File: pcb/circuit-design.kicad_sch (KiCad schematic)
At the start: 8 parts, among them J1 USB_C_Receptacle_USB2.0_16P, U1 USBLC6-2SC6

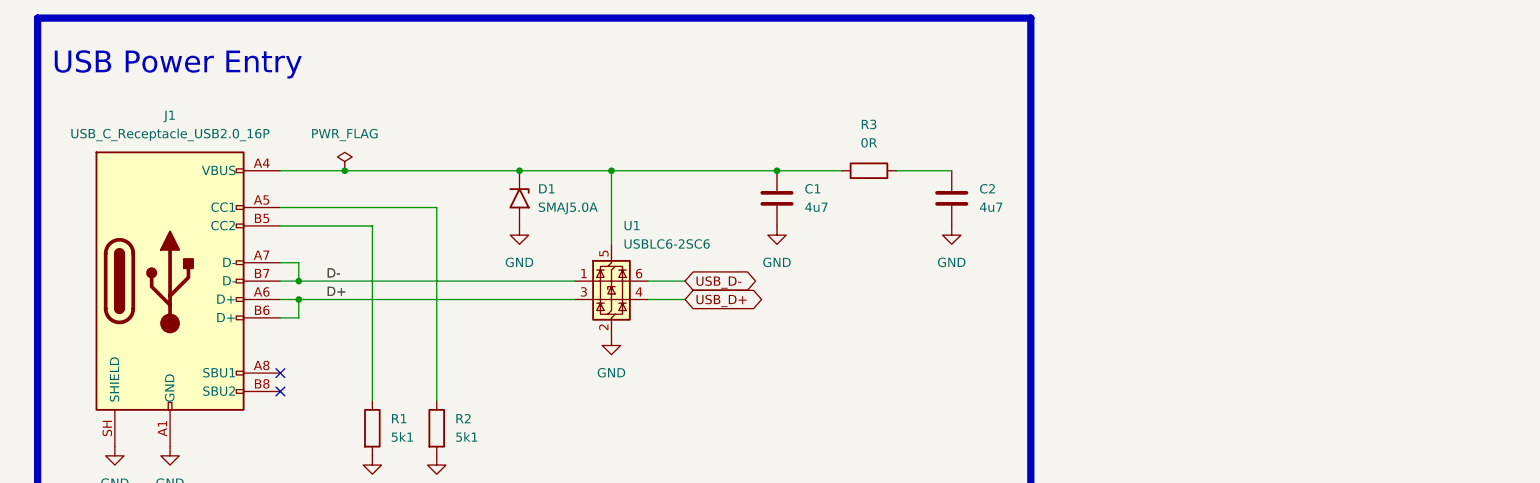
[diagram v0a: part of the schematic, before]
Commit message: feat(sch/pwr): add 3.3V LDO regulation circuit
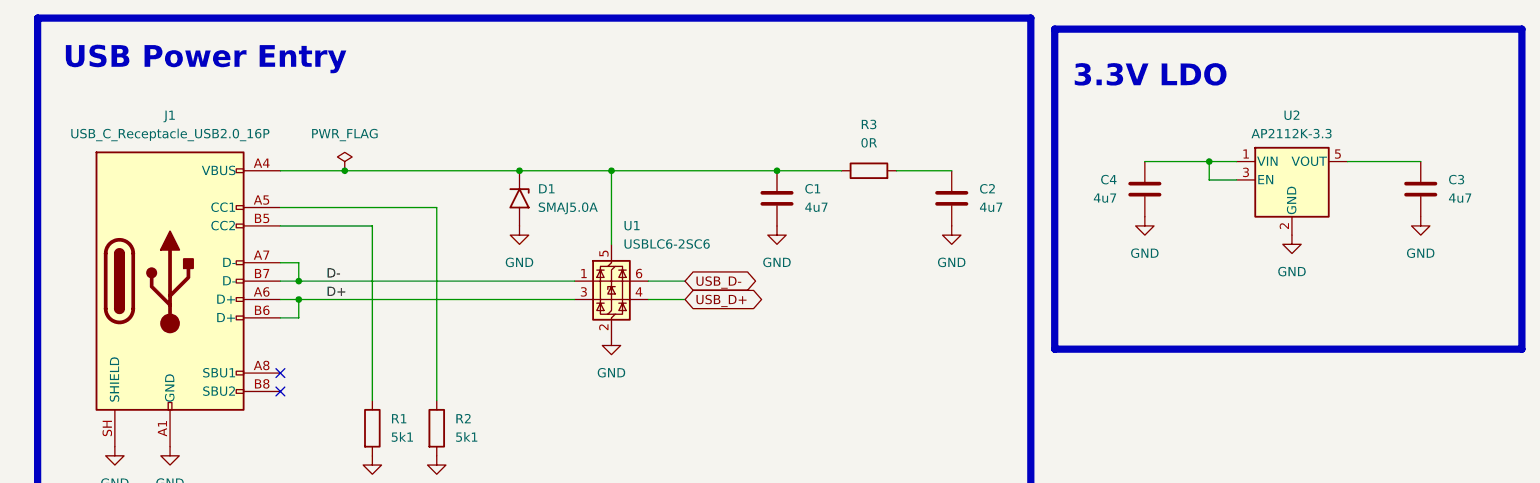
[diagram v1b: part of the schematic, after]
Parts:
- added C3, C4: 4u7, Package_TO_SOT_SMD:SOT-23-5, symbol Device:C
- added U2: AP2112K-3.3, Package_TO_SOT_SMD:SOT-23-5, symbol Regulator_Linear:AP2112K-3.3
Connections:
- net GND: now also C3.2, C4.2, U2.2 (GND)
- new net: C4.1, U2.1 (VIN), U2.3 (EN)
- new net: C3.1, U2.5 (VOUT)
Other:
- note added: "3.3V LDO"

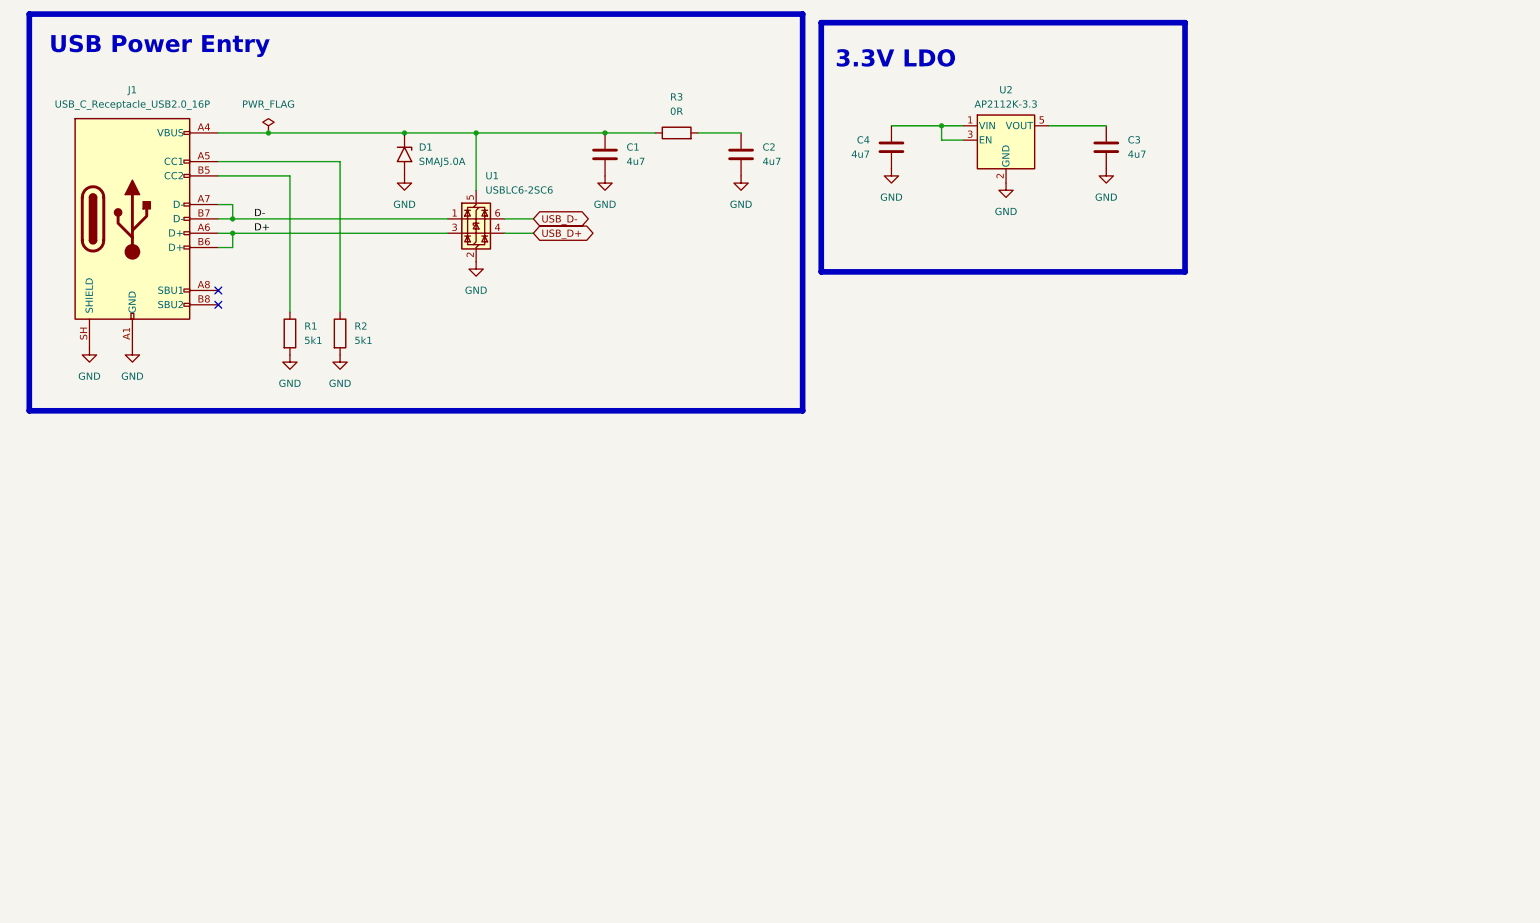
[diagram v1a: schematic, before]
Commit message: feat(sch/mcu): add mcu and auxiliary circuits
There were added the fundamental MCU circuits:
- Power conditioning
- Boot
- Reset/Enable (is the same for ESP32 MCUs)
- Clock
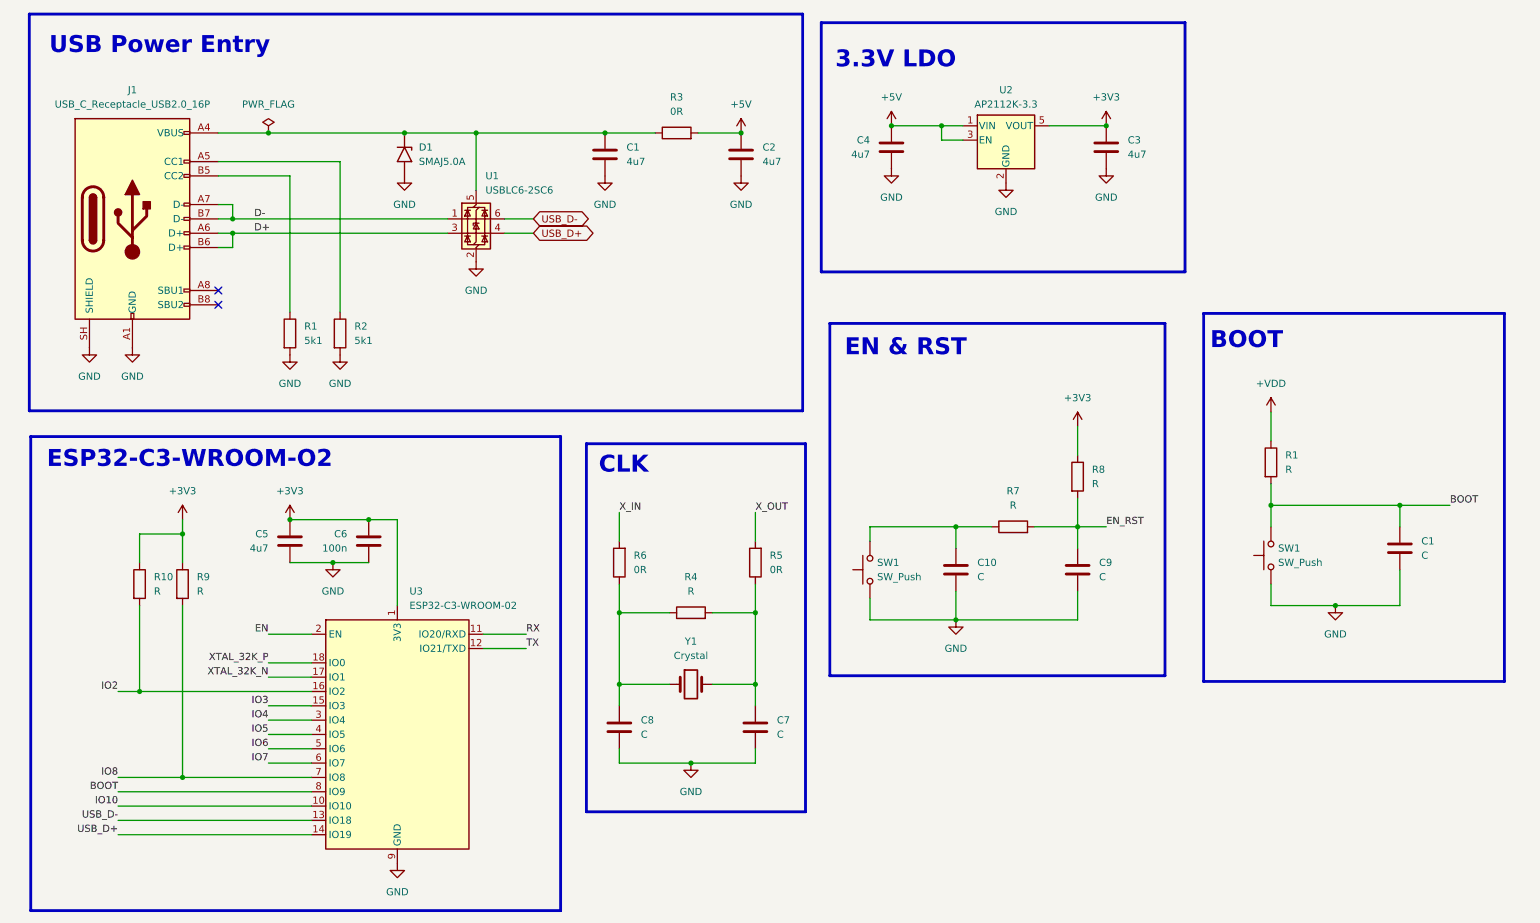
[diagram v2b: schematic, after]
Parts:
- added C1, C10, C7, C8, C9: C, symbol Device:C
- added C5: 4u7, Diode_SMD:D_SMA, symbol Device:C
- added C6: 100n, Diode_SMD:D_SMA, symbol Device:C
- added R1, R10, R4, R7, R8, R9: R, symbol Device:R
- added R5, R6: 0R, symbol Device:R
- added SW1 (x2): SW_Push, Button_Switch_SMD:Nidec_Copal_CAS-120A, symbol Switch:SW_Push
- added U3: ESP32-C3-WROOM-02, RF_Module:ESP32-C3-WROOM-02, symbol RF_Module:ESP32-C3-WROOM-02
- added Y1: Crystal, AMDY:XTAL_EPSON_TSX-3225, symbol Device:Crystal
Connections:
- net GND: now also C1.2, C10.2, C5.2, C6.2, C7.2, C8.2, C9.2, SW1.1, SW1.1, U3.19 (GND), U3.9 (GND)
- net USB_D+: now also U3.14 (IO19)
- net USB_D-: now also U3.13 (IO18)
- net +5V: now reaches C2.1, R3.2
- net +5V: now also C4.1, U2.1 (VIN), U2.3 (EN)
- net +3V3: now reaches C3.1, U2.5 (VOUT)
- net +3V3: now also C5.1, C6.1, R10.1, R8.1, R9.1, U3.1 (3V3)
- new net: C7.1, R4.2, R5.1, Y1.2
- new net: C8.1, R4.1, R6.1, Y1.1
- new net: C10.1, R7.1, SW1.2
- new net +VDD: R1.1
- new net BOOT: C1.1, R1.2, SW1.2, U3.8 (IO9)
- new net EN: U3.2 (EN)
- new net EN_RST: C9.1, R7.2, R8.2
- new net IO10: U3.10 (IO10)
- new net IO2: R10.2, U3.16 (IO2)
- new net IO3: U3.15 (IO3)
- new net IO4: U3.3 (IO4)
- new net IO5: U3.4 (IO5)
- new net IO6: U3.5 (IO6)
- new net IO7: U3.6 (IO7)
- new net IO8: R9.2, U3.7 (IO8)
- new net RX: U3.11 (IO20/RXD)
- new net TX: U3.12 (IO21/TXD)
- new net XTAL_32K_N: U3.17 (IO1)
- new net XTAL_32K_P: U3.18 (IO0)
- new net X_IN: R6.2
- new net X_OUT: R5.2
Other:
- note added: "BOOT"
- note added: "CLK"
- note added: "EN & RST"
- note added: "ESP32-C3-WROOM-O2"

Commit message: feat(sch/io): add gpio expansion headers
In addition to access the IO ESP32 pins, excluding strapping pins (IO2, IO8), USB data lines (IO18, IO19) and XTAL pins (IO0, IO1), there are also included +5V and +3V3 and 3 extra GND pins.
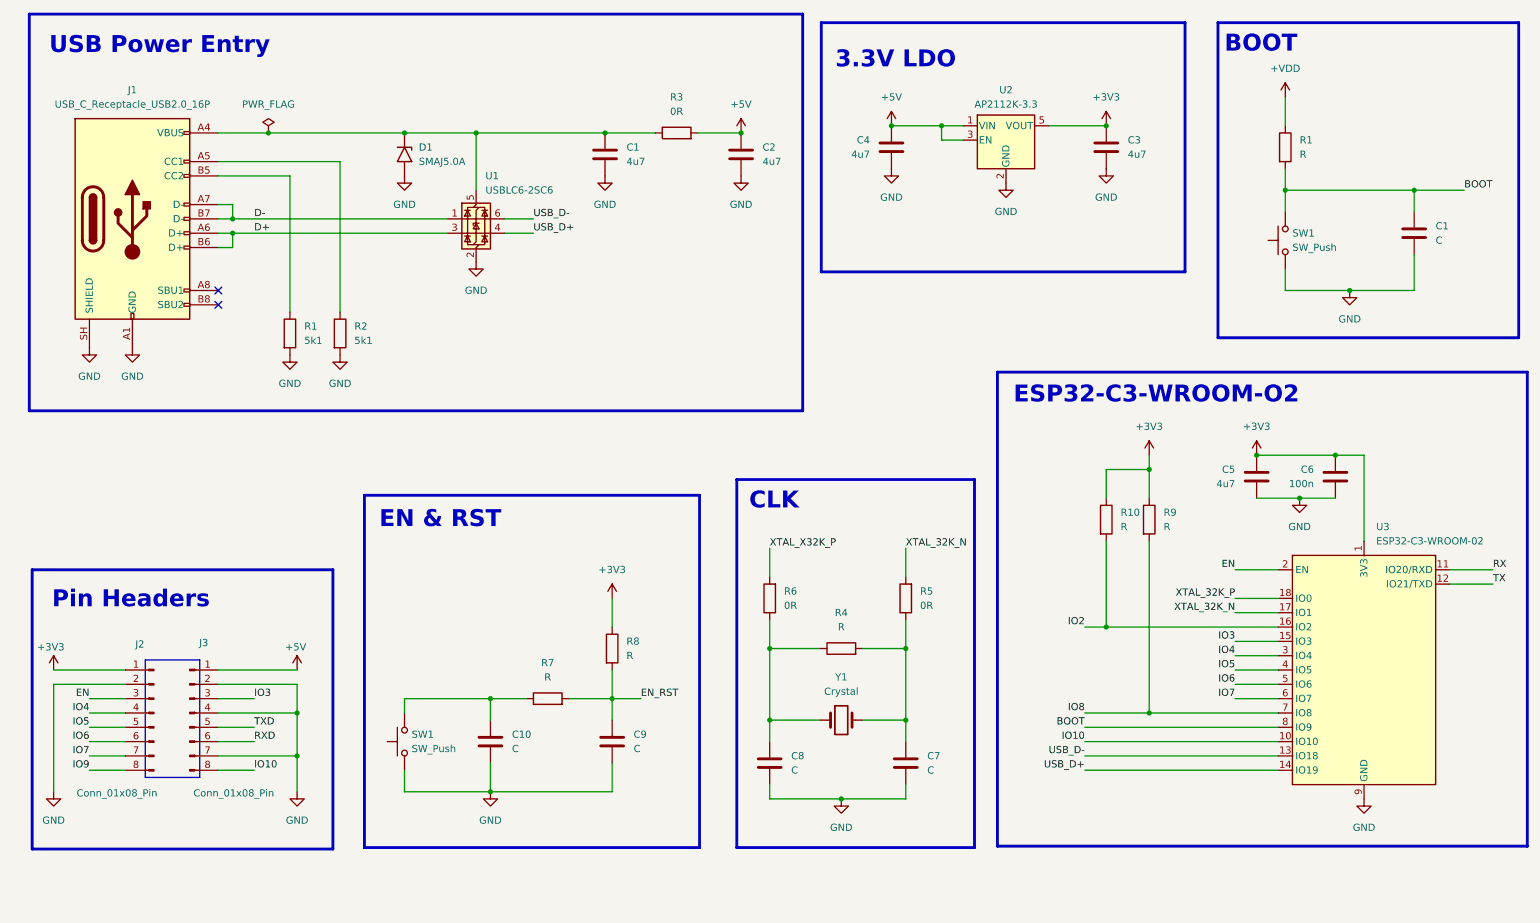
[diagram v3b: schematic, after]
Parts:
- added J2, J3: Conn_01x08_Pin, Connector_PinHeader_2.54mm:PinHeader_1x08_P2.54mm_Vertical, symbol Connector:Conn_01x08_Pin
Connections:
- net X_OUT is gone; now on net XTAL_32K_N: R5.2
- net +3V3: now also J2.1 (Pin_1)
- net +5V: now also J3.1 (Pin_1)
- net EN: now also J2.3 (Pin_3)
- net GND: now also J2.2 (Pin_2), J3.2 (Pin_2), J3.4 (Pin_4), J3.7 (Pin_7)
- net IO10: now also J3.8 (Pin_8)
- net IO3: now also J3.3 (Pin_3)
- net IO4: now also J2.4 (Pin_4)
- net IO5: now also J2.5 (Pin_5)
- net IO6: now also J2.6 (Pin_6)
- net IO7: now also J2.7 (Pin_7)
- net X_IN renamed XTAL_X32K_P
- new net IO9: J2.8 (Pin_8)
- new net RXD: J3.6 (Pin_6)
- new net TXD: J3.5 (Pin_5)
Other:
- note added: "Pin Headers"
- moved on the sheet: C1, C10, C5, C6, C7, C8, C9, R1, R10, R4, R5, R6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

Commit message: feat(lay): add first placement of all parts
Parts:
- C1: renamed from C10; footprint (none) -> Capacitor_SMD:C_0603_1608Metric
- C10: renamed from C6; footprint Diode_SMD:D_SMA -> Capacitor_SMD:C_0603_1608Metric
- C11: renamed from C1; footprint (none) -> Capacitor_SMD:C_0603_1608Metric
- C2: renamed from C1; footprint Diode_SMD:D_SMA -> Capacitor_SMD:C_0603_1608Metric
- C3: renamed from C9; footprint (none) -> Capacitor_SMD:C_0603_1608Metric
- C4: renamed from C2; footprint Diode_SMD:D_SMA -> Capacitor_SMD:C_0603_1608Metric
- C5: renamed from C8; footprint (none) -> Capacitor_SMD:C_0603_1608Metric
- C6: renamed from C4; footprint Package_TO_SOT_SMD:SOT-23-5 -> Capacitor_SMD:C_0603_1608Metric
- C7: footprint (none) -> Capacitor_SMD:C_0603_1608Metric
- C8: renamed from C3; footprint Package_TO_SOT_SMD:SOT-23-5 -> Capacitor_SMD:C_0603_1608Metric
- C9: renamed from C5; footprint Diode_SMD:D_SMA -> Capacitor_SMD:C_0603_1608Metric
- R1, R2: footprint Resistor_SMD:R_0402_1005Metric -> Resistor_SMD:R_0603_1608Metric
- R10: renamed from R9; footprint (none) -> Resistor_SMD:R_0603_1608Metric
- R11: renamed from R1; footprint (none) -> Resistor_SMD:R_0603_1608Metric
- R3: renamed from R7; footprint (none) -> Resistor_SMD:R_0603_1608Metric
- R4: renamed from R8; footprint (none) -> Resistor_SMD:R_0603_1608Metric
- R5: renamed from R3; footprint (none) -> Resistor_SMD:R_0603_1608Metric
- R6: footprint (none) -> Resistor_SMD:R_0603_1608Metric
- R7: renamed from R4; footprint (none) -> Resistor_SMD:R_0603_1608Metric
- R8: renamed from R5; footprint (none) -> Resistor_SMD:R_0603_1608Metric
- R9: renamed from R10; footprint (none) -> Resistor_SMD:R_0603_1608Metric
- SW1: footprint Button_Switch_SMD:Nidec_Copal_CAS-120A -> Button_Switch_SMD:SW_SPST_B3U-1000P
- SW2: renamed from SW1; footprint Button_Switch_SMD:Nidec_Copal_CAS-120A -> Button_Switch_SMD:SW_SPST_B3U-1000P
- Y1: footprint AMDY:XTAL_EPSON_TSX-3225 -> Crystal:Crystal_SMD_3215-2Pin_3.2x1.5mm
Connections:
- net IO9 is gone; now on net BOOT: J2.8 (Pin_8)
- net RX is gone; now on net RXD: U3.11 (IO20/RXD)
- net TX is gone; now on net TXD: U3.12 (IO21/TXD)
- net XTAL_X32K_P is gone; now on net XTAL_32K_P: R6.2
- net IO2: no longer names the net of R9.2, U3.16 (IO2)
- net IO8: no longer names the net of R10.2, U3.7 (IO8)
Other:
- moved on the sheet: C11, C6, C8, R11, SW2, U2
